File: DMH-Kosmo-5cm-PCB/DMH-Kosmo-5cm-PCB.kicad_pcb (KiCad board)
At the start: 2 copper layers, 48 x 175 mm, 0 parts

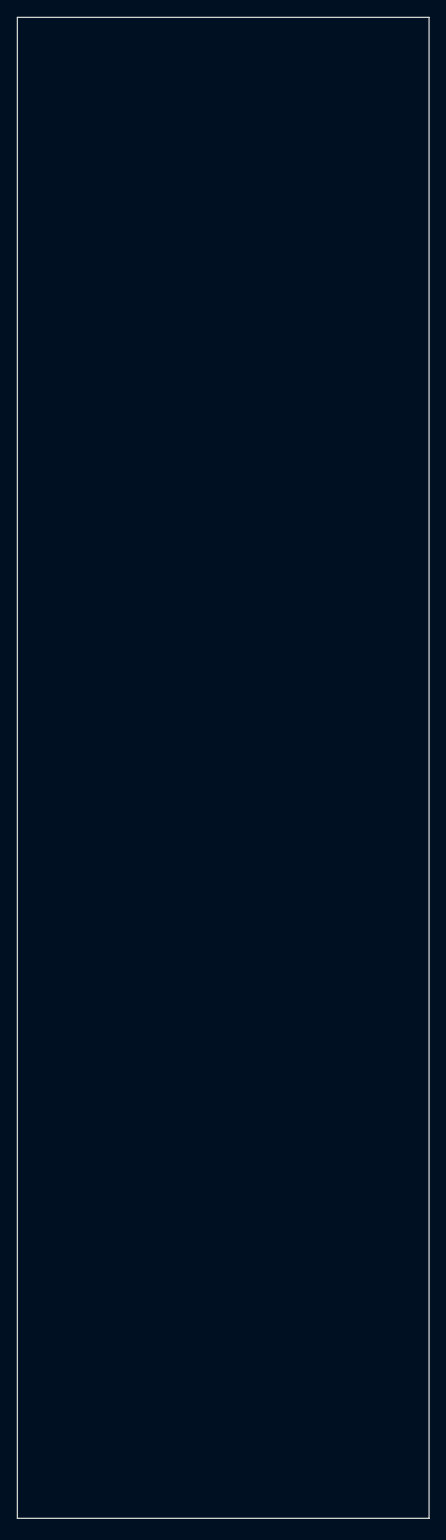
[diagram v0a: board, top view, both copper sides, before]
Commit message: Finished 5cm Panel template
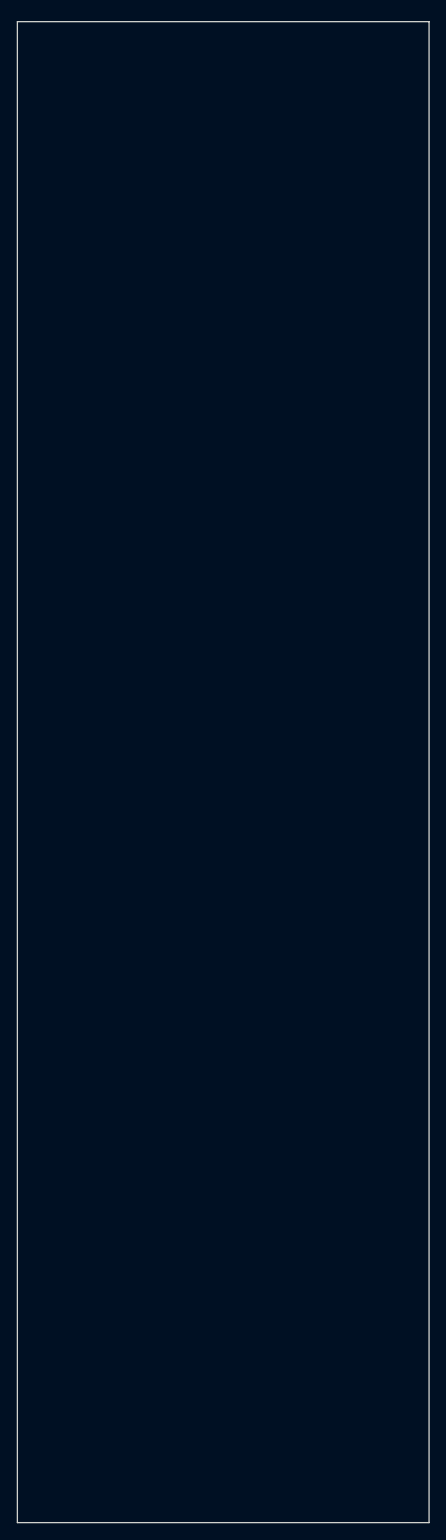
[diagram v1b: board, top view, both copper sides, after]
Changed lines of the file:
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@@
 	(net 0 "")
 	(gr_rect
-		(start 51 42)
-		(end 99 217)
+		(start 51 42.5)
+		(end 99 217.5)
 		(stroke
 			(width 0.05)

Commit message: Updated 5cm and 10 templates
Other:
- board text added: "Mk1.0 - Month Year"
- board text removed: "JLCJLCJLCJLC"
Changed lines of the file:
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@@
 	(net 0 "")
+	(gr_rect
+		(start 70 212.75)
+		(end 80 214.75)
+		(stroke
+			(width 0.1)
+			(type solid)
+		)
+		(fill solid)
+		(layer "B.SilkS")
+	)
 	(gr_rect
 		(start 51 42.5)
@@
 		(layer "User.9")
 	)
-	(gr_text "JLCJLCJLCJLC"
-		(at 75 45 0)
+	(gr_text "Mk1.0 - Month Year"
+		(at 74.75 216.25 0)
 		(layer "B.SilkS")
 		(effects
 			(font
 				(size 1 1)
-				(thickness 0.15)
+				(thickness 0.25)
+				(bold yes)
 			)
 			(justify mirror)
